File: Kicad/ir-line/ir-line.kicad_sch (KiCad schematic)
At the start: 28 parts, among them IC1 VISHAY-CNY70, IC2 VISHAY-CNY70, IC3 VISHAY-CNY70, IC4 VISHAY-CNY70, IC5 VISHAY-CNY70, IC6 TPS92612, IC7 TPS92612, K1 FRONT #1, K2 FRONT #2

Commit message: Draft
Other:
- note added: "DRAFT"
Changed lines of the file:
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@@
     (effects (font (size 1.27 1.27)) (justify left bottom))
+  )
+  (text "DRAFT" (at 210.82 190.5 0)
+    (effects (font (size 5 5)) (justify left bottom))
   )
   (text "(10n)" (at 154.94 109.22 0)

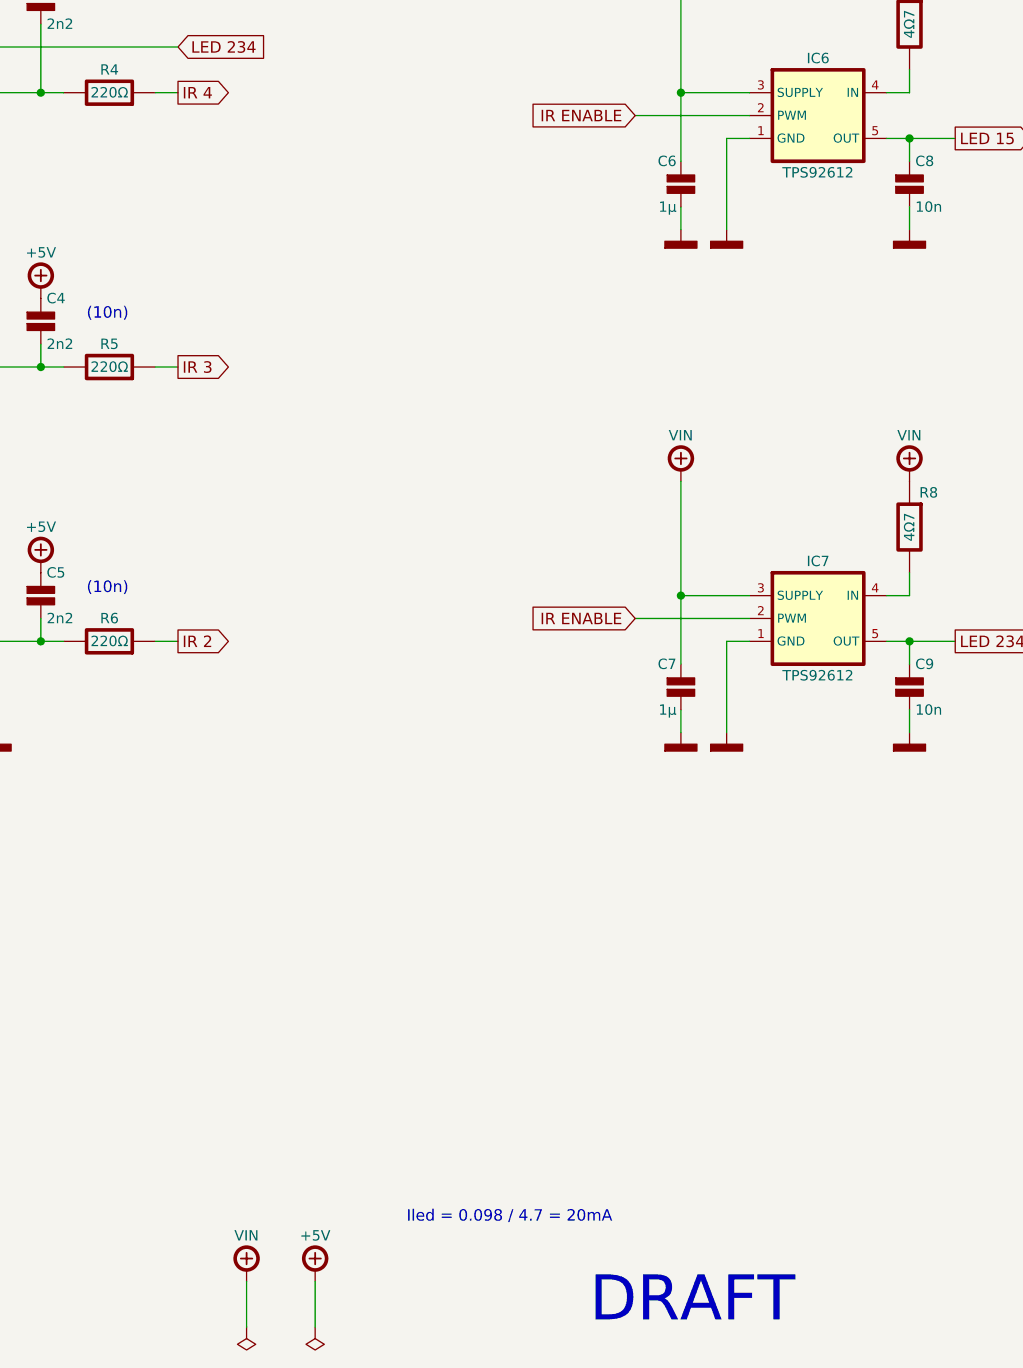
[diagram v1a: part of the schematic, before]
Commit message: Update IR Line
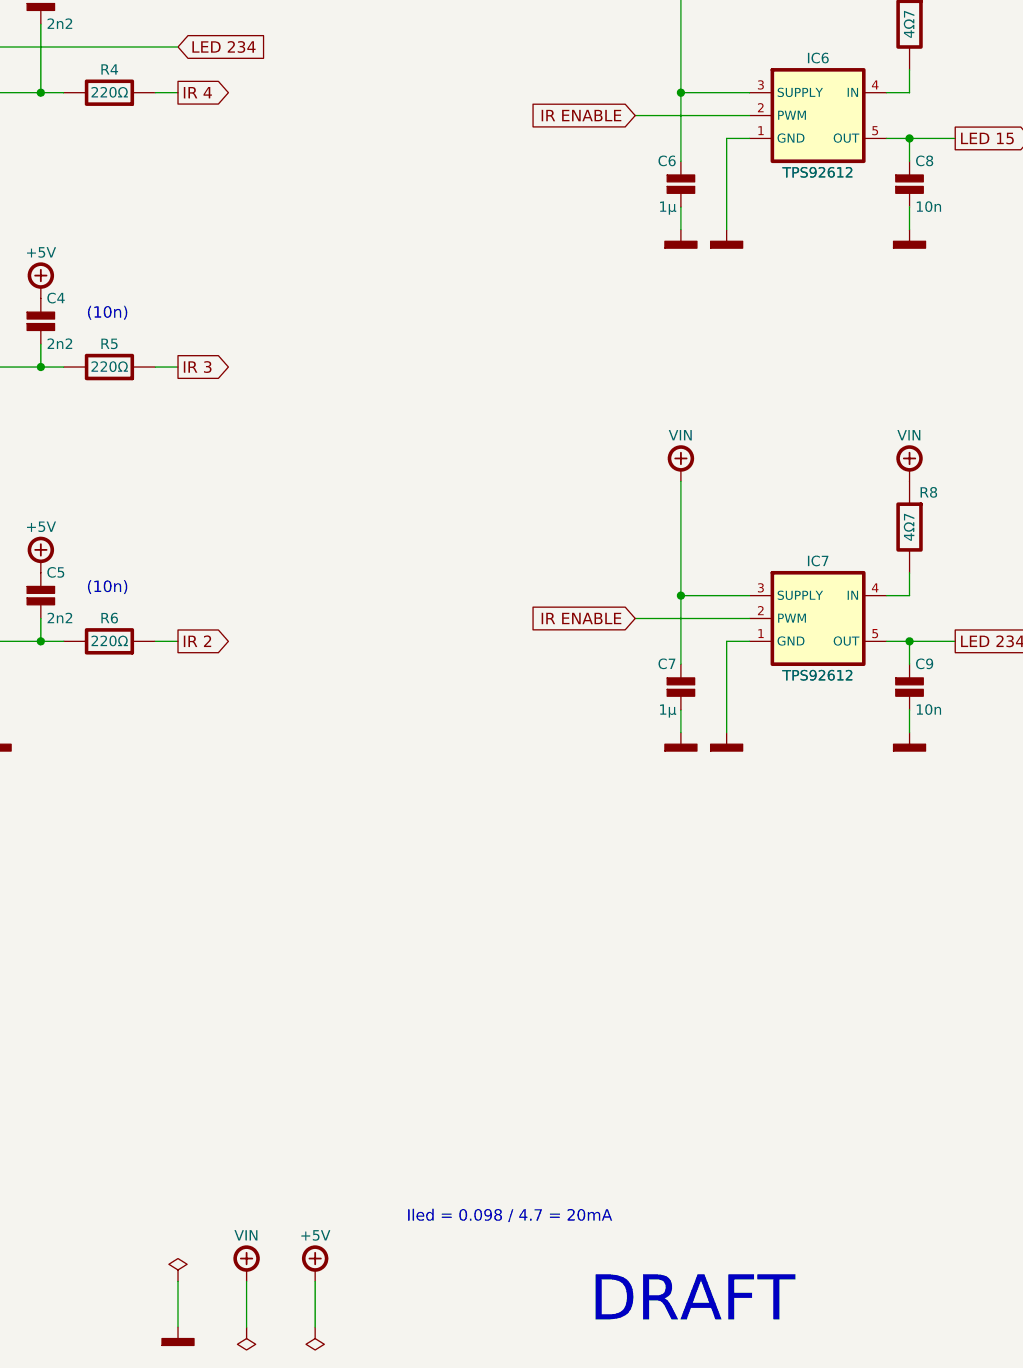
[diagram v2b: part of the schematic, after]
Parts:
- IC1, IC2, IC3, IC4, IC5: MOUSER 782-CNY70 -> (none); Mouser (none) -> 782-CNY70
- IC6, IC7: symbol tronixio:TPS92612 -> tronixio:TI-TPS92612; MOUSER 595-TPS92612DBVR -> (none); Mouser (none) -> 595-TPS92612DBVR; Name (none) -> TPS92612
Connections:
- net GND: now also IC1.4 (EMITTER), IC2.2 (CATHODE), IC2.4 (EMITTER), IC3.4 (EMITTER), IC4.4 (EMITTER), IC5.2 (CATHODE), IC5.4 (EMITTER); no longer IC1.3 (E), IC2.1 (K), IC2.3 (E), IC3.3 (E), IC4.3 (E), IC5.1 (K), IC5.3 (E)
- net LED 15: now also IC1.1 (ANODE); no longer IC1.4 (A)
- net LED 234: now also IC3.1 (ANODE); no longer IC3.4 (A)
- net at C3.2, R4.1: now also IC3.3 (COLLECTOR); no longer IC3.2 (C)
- net at C4.2, R5.1: now also IC4.3 (COLLECTOR); no longer IC4.2 (C)
- net at C1.2, R2.1: now also IC1.3 (COLLECTOR); no longer IC1.2 (C)
- net at C5.2, R6.1: now also IC5.3 (COLLECTOR); no longer IC5.2 (C)
- net at C2.2, R3.1: now also IC2.3 (COLLECTOR); no longer IC2.2 (C)
- net at IC4.1 (ANODE): now also IC3.2 (CATHODE); no longer IC5.4 (A)
- new net: IC1.2 (CATHODE), IC2.1 (ANODE)
- new net: IC4.2 (CATHODE), IC5.1 (ANODE)
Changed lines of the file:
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@@
     (stroke (width 0) (type solid) (color 0 0 0 0))
+  )
+  (wire (pts (xy 165.1 185.42) (xy 165.1 190.5))
+    (stroke (width 0) (type default) (color 0 0 0 0))
   )
   (wire (pts (xy 53.34 53.34) (xy 66.04 53.34))
@@
     )
     (property "Value" "VISHAY-CNY70" (id 1) (at 132.08 62.23 0)
-      (effects (font (size 1 1)) hide)
-    )
-    (property "Footprint" "tronixio:VISHAY-CNY70" (id 2) (at 132.08 62.23 0)
+      (effects (font (size 1.15 1.15)) hide)
+    )
+    (property "Footprint" "tronixio:VISHAY-CNY70" (id 2) (at 132.08 64.77 0)
       (effects (font (size 1 1)) hide)
     )
@@
       (effects (font (size 1 1)) hide)
     )
-    (property "MOUSER" "782-CNY70" (id 4) (at 132.08 69.85 0)
-      (effects (font (size 1 1)) hide)
-    )
     (property "Name" "CNY70" (id 5) (at 132.08 58.42 0)
       (effects (font (size 1.15 1.15)))
+    )
+    (property "Mouser" "782-CNY70" (id 6) (at 132.08 69.85 0)
+      (effects (font (size 1 1)) hide)
     )
     (pin "1")
@@
     (pin "1")
   )
-  (symbol (lib_id "tronixio:TPS92612") (at 236.22 111.76 0) (unit 1)
+  (symbol (lib_id "tronixio:TI-TPS92612") (at 236.22 111.76 0) (unit 1)
     (in_bom yes) (on_board yes)
     (property "Reference" "IC7" (id 0) (at 236.22 105.41 0)
@@
       (effects (font (size 1 1)) hide)
     )
-    (property "MOUSER" "595-TPS92612DBVR" (id 4) (at 236.22 127 0)
+    (property "Name" "TPS92612" (id 4) (at 236.22 118.11 0)
+      (effects (font (size 1.15 1.15)))
+    )
+    (property "Mouser" "595-TPS92612DBVR" (id 5) (at 236.22 129.54 0)
       (effects (font (size 1 1)) hide)
     )
@@
     )
     (property "Value" "VISHAY-CNY70" (id 1) (at 48.26 62.23 0)
-      (effects (font (size 1 1)) hide)
-    )
-    (property "Footprint" "tronixio:VISHAY-CNY70" (id 2) (at 48.26 62.23 0)
+      (effects (font (size 1.15 1.15)) hide)
+    )
+    (property "Footprint" "tronixio:VISHAY-CNY70" (id 2) (at 48.26 64.77 0)
       (effects (font (size 1 1)) hide)
     )
@@
       (effects (font (size 1 1)) hide)
     )
-    (property "MOUSER" "782-CNY70" (id 4) (at 48.26 69.85 0)
-      (effects (font (size 1 1)) hide)
-    )
     (property "Name" "CNY70" (id 5) (at 48.26 58.42 0)
       (effects (font (size 1.15 1.15)))
+    )
+    (property "Mouser" "782-CNY70" (id 6) (at 48.26 69.85 0)
+      (effects (font (size 1 1)) hide)
     )
     (pin "1")
@@
     (pin "1")
   )
+  (symbol (lib_id "tronixio:PWR_FLAG") (at 165.1 185.42 0) (unit 1)
+    (in_bom yes) (on_board yes) (fields_autoplaced)
+    (property "Reference" "#FLG01" (id 0) (at 165.1 187.325 0)
+      (effects (font (size 1.27 1.27)) hide)
+    )
+    (property "Value" "PWR_FLAG" (id 1) (at 165.1 189.23 0)
+      (effects (font (size 1.27 1.27)) hide)
+    )
+    (property "Footprint" "" (id 2) (at 165.1 185.42 0)
+      (effects (font (size 1.27 1.27)) hide)
+    )
+    (property "Datasheet" "~" (id 3) (at 165.1 185.42 0)
+      (effects (font (size 1.27 1.27)) hide)
+    )
+    (pin "1")
+  )
   (symbol (lib_id "tronixio:POWER-VIN") (at 220.98 40.64 0) (unit 1)
     (in_bom yes) (on_board yes)
@@
     (pin "2")
   )
+  (symbol (lib_id "tronixio:POWER-GND") (at 165.1 190.5 0) (unit 1)
+    (in_bom yes) (on_board yes)
+    (property "Reference" "#PWR015" (id 0) (at 165.1 195.58 0)
+      (effects (font (size 1 1)) hide)
+    )
+    (property "Value" "POWER-GND" (id 1) (at 165.1 198.12 0)
+      (effects (font (size 1 1)) hide)
+    )
+    (property "Footprint" "" (id 2) (at 165.1 190.5 0)
+      (effects (font (size 1 1)) hide)
+    )
+    (property "Datasheet" "" (id 3) (at 165.1 190.5 0)
+      (effects (font (size 1 1)) hide)
+    )
+    (pin "1")
+  )
   (symbol (lib_id "tronixio:POWER-GND") (at 226.06 124.46 0) (unit 1)
     (in_bom yes) (on_board yes)
@@
     (pin "1")
   )
-  (symbol (lib_id "tronixio:TPS92612") (at 236.22 55.88 0) (unit 1)
+  (symbol (lib_id "tronixio:TI-TPS92612") (at 236.22 55.88 0) (unit 1)
     (in_bom yes) (on_board yes)
     (property "Reference" "IC6" (id 0) (at 236.22 49.53 0)
@@
       (effects (font (size 1 1)) hide)
     )
-    (property "MOUSER" "595-TPS92612DBVR" (id 4) (at 236.22 71.12 0)
+    (property "Name" "TPS92612" (id 4) (at 236.22 62.23 0)
+      (effects (font (size 1.15 1.15)))
+    )
+    (property "Mouser" "595-TPS92612DBVR" (id 5) (at 236.22 73.66 0)
       (effects (font (size 1 1)) hide)
     )
@@
     )
     (property "Value" "VISHAY-CNY70" (id 1) (at 48.26 92.71 0)
-      (effects (font (size 1 1)) hide)
-    )
-    (property "Footprint" "tronixio:VISHAY-CNY70" (id 2) (at 48.26 92.71 0)
+      (effects (font (size 1.15 1.15)) hide)
+    )
+    (property "Footprint" "tronixio:VISHAY-CNY70" (id 2) (at 48.26 95.25 0)
       (effects (font (size 1 1)) hide)
     )
@@
       (effects (font (size 1 1)) hide)
     )
-    (property "MOUSER" "782-CNY70" (id 4) (at 48.26 100.33 0)
-      (effects (font (size 1 1)) hide)
-    )
     (property "Name" "CNY70" (id 5) (at 48.26 88.9 0)
       (effects (font (size 1.15 1.15)))
+    )
+    (property "Mouser" "782-CNY70" (id 6) (at 48.26 100.33 0)
+      (effects (font (size 1 1)) hide)
     )
     (pin "1")
@@
     )
     (property "Value" "VISHAY-CNY70" (id 1) (at 132.08 123.19 0)
-      (effects (font (size 1 1)) hide)
-    )
-    (property "Footprint" "tronixio:VISHAY-CNY70" (id 2) (at 132.08 123.19 0)
+      (effects (font (size 1.15 1.15)) hide)
+    )
+    (property "Footprint" "tronixio:VISHAY-CNY70" (id 2) (at 132.08 125.73 0)
       (effects (font (size 1 1)) hide)
     )
@@
       (effects (font (size 1 1)) hide)
     )
-    (property "MOUSER" "782-CNY70" (id 4) (at 132.08 130.81 0)
-      (effects (font (size 1 1)) hide)
-    )
     (property "Name" "CNY70" (id 5) (at 132.08 119.38 0)
       (effects (font (size 1.15 1.15)))
+    )
+    (property "Mouser" "782-CNY70" (id 6) (at 132.08 130.81 0)
+      (effects (font (size 1 1)) hide)
     )
     (pin "1")
@@
     )
     (property "Value" "VISHAY-CNY70" (id 1) (at 132.08 92.71 0)
-      (effects (font (size 1 1)) hide)
-    )
-    (property "Footprint" "tronixio:VISHAY-CNY70" (id 2) (at 132.08 92.71 0)
+      (effects (font (size 1.15 1.15)) hide)
+    )
+    (property "Footprint" "tronixio:VISHAY-CNY70" (id 2) (at 132.08 95.25 0)
       (effects (font (size 1 1)) hide)
     )
@@
       (effects (font (size 1 1)) hide)
     )
-    (property "MOUSER" "782-CNY70" (id 4) (at 132.08 100.33 0)
-      (effects (font (size 1 1)) hide)
-    )
     (property "Name" "CNY70" (id 5) (at 132.08 88.9 0)
       (effects (font (size 1.15 1.15)))
+    )
+    (property "Mouser" "782-CNY70" (id 6) (at 132.08 100.33 0)
+      (effects (font (size 1 1)) hide)
     )
     (pin "1")
@@
   )
   (symbol_instances
+    (path "/4442bbd3-d8c0-4204-a455-7ee1bc0d1e7f"
+      (reference "#FLG01") (unit 1) (value "PWR_FLAG") (footprint "")
+    )
     (path "/04e01352-a943-422f-843f-398a5122f31f"
       (reference "#FLG02") (unit 1) (value "PWR_FLAG") (footprint "")
@@
       (reference "#PWR014") (unit 1) (value "POWER-+5V") (footprint "")
     )
+    (path "/63a484a7-e75f-4f97-ac14-1ebad1b80741"
+      (reference "#PWR015") (unit 1) (value "POWER-GND") (footprint "")
+    )
     (path "/55d71a0a-a0b9-4237-b11f-ba473c6f7312"

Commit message: Update
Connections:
- net +5V renamed VCC
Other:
- note added: "VDD: 3V3 or 5V."
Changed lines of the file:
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@@
     (effects (font (size 1.27 1.27)) (justify left bottom))
   )
-  (text "Iled = 0.098 / 4.7 = 20mA" (at 213.36 179.07 180)
-    (effects (font (size 1.27 1.27)) (justify right bottom))
+  (text "VDD: 3V3 or 5V." (at 185.42 176.53 0)
+    (effects (font (size 1.27 1.27)) (justify left bottom))
   )
   (text "(10n)" (at 154.94 43.18 0)
@@
   (text "DRAFT" (at 210.82 190.5 0)
     (effects (font (size 5 5)) (justify left bottom))
+  )
+  (text "Iled = 0.098 / 4.7 = 20mA" (at 185.42 179.07 0)
+    (effects (font (size 1.27 1.27)) (justify left bottom))
   )
   (text "(10n)" (at 154.94 109.22 0)
@@
     (pin "1")
   )
-  (symbol (lib_id "tronixio:POWER-+5V") (at 149.86 76.2 0) (unit 1)
+  (symbol (lib_id "tronixio:POWER-VDD") (at 149.86 76.2 0) (unit 1)
     (in_bom yes) (on_board yes)
     (property "Reference" "#PWR013" (id 0) (at 149.86 86.36 0)
@@
       (effects (font (size 1 1)) hide)
     )
-    (property "Name" "+5V" (id 4) (at 149.86 71.12 0)
-      (effects (font (size 1.15 1.15)))
-    )
-    (pin "1")
-  )
-  (symbol (lib_id "tronixio:POWER-+5V") (at 66.04 40.64 0) (unit 1)
+    (property "Name" "VDD" (id 4) (at 149.86 71.12 0)
+      (effects (font (size 1.15 1.15)))
+    )
+    (pin "1")
+  )
+  (symbol (lib_id "tronixio:POWER-VDD") (at 66.04 40.64 0) (unit 1)
     (in_bom yes) (on_board yes)
     (property "Reference" "#PWR06" (id 0) (at 66.04 50.8 0)
       (effects (font (size 1 1)) hide)
     )
-    (property "Value" "POWER-+5V" (id 1) (at 66.04 53.34 0)
+    (property "Value" "" (id 1) (at 66.04 53.34 0)
       (effects (font (size 1 1)) hide)
     )
@@
       (effects (font (size 1 1)) hide)
     )
-    (property "Name" "+5V" (id 4) (at 66.04 35.56 0)
+    (property "Name" "VDD" (id 4) (at 66.04 35.56 0)
       (effects (font (size 1.15 1.15)))
     )
@@
     (pin "1")
   )
-  (symbol (lib_id "tronixio:POWER-+5V") (at 149.86 40.64 0) (unit 1)
+  (symbol (lib_id "tronixio:POWER-VDD") (at 149.86 40.64 0) (unit 1)
     (in_bom yes) (on_board yes)
     (property "Reference" "#PWR012" (id 0) (at 149.86 50.8 0)
@@
       (effects (font (size 1 1)) hide)
     )
-    (property "Name" "+5V" (id 4) (at 149.86 35.56 0)
+    (property "Name" "VDD" (id 4) (at 149.86 35.56 0)
       (effects (font (size 1.15 1.15)))
     )
@@
     (pin "5")
   )
-  (symbol (lib_id "tronixio:POWER-+5V") (at 180.34 185.42 0) (unit 1)
+  (symbol (lib_id "tronixio:POWER-VDD") (at 180.34 185.42 0) (unit 1)
     (in_bom yes) (on_board yes)
     (property "Reference" "#PWR017" (id 0) (at 180.34 195.58 0)
@@
       (effects (font (size 1 1)) hide)
     )
-    (property "Name" "+5V" (id 4) (at 180.34 180.34 0)
+    (property "Name" "VDD" (id 4) (at 180.34 180.34 0)
       (effects (font (size 1.15 1.15)))
     )
@@
     (pin "1")
   )
-  (symbol (lib_id "tronixio:POWER-+5V") (at 149.86 106.68 0) (unit 1)
+  (symbol (lib_id "tronixio:POWER-VDD") (at 149.86 106.68 0) (unit 1)
     (in_bom yes) (on_board yes)
     (property "Reference" "#PWR014" (id 0) (at 149.86 116.84 0)
@@
       (effects (font (size 1 1)) hide)
     )
-    (property "Name" "+5V" (id 4) (at 149.86 101.6 0)
+    (property "Name" "VDD" (id 4) (at 149.86 101.6 0)
       (effects (font (size 1.15 1.15)))
     )
@@
     (pin "1")
   )
-  (symbol (lib_id "tronixio:POWER-+5V") (at 66.04 76.2 0) (unit 1)
+  (symbol (lib_id "tronixio:POWER-VDD") (at 66.04 76.2 0) (unit 1)
     (in_bom yes) (on_board yes)
     (property "Reference" "#PWR07" (id 0) (at 66.04 86.36 0)
@@
       (effects (font (size 1 1)) hide)
     )
-    (property "Name" "+5V" (id 4) (at 66.04 71.12 0)
+    (property "Name" "VDD" (id 4) (at 66.04 71.12 0)
       (effects (font (size 1.15 1.15)))
     )
@@
     (pin "2")
   )
-  (symbol (lib_id "tronixio:POWER-+5V") (at 91.44 144.78 0) (unit 1)
+  (symbol (lib_id "tronixio:POWER-VDD") (at 91.44 144.78 0) (unit 1)
     (in_bom yes) (on_board yes)
     (property "Reference" "#PWR08" (id 0) (at 91.44 154.94 0)
@@
       (effects (font (size 1 1)) hide)
     )
-    (property "Name" "+5V" (id 4) (at 91.44 139.7 0)
-      (effects (font (size 1.15 1.15)))
-    )
+    (property "Name" "VDD" (id 4) (at 91.44 139.7 0)
+      (effects (font (size 1.15 1.15)))
+    )

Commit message: Update
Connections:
- net VCC renamed +5V
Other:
- moved on the sheet: C1, C2, C3, C4, C5, C6, C7, C8, C9, IC1, IC2, IC3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

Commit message: Update
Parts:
- C1, C2, C3, C4, C5: footprint tronixio:CAPACITOR-1206 -> tronixio:CAPACITOR-SMD-1206; symbol tronixio:C-1206 -> tronixio:CAPACITOR-1206-2N2-10P-X7R; Mouser (none) -> 80-C1206C222K5R; Tolerance (none) -> 10%; Voltage (none) -> 50V
- C6, C7: footprint tronixio:CAPACITOR-1206 -> tronixio:CAPACITOR-SMD-1206; symbol tronixio:C-1206 -> tronixio:CAPACITOR-1206-1U-10P-X7R; Mouser (none) -> 80-C1206C105K4R; Tolerance (none) -> 10%; Voltage (none) -> 16V
- C8, C9: footprint tronixio:CAPACITOR-1206 -> tronixio:CAPACITOR-SMD-1206; symbol tronixio:C-1206 -> tronixio:CAPACITOR-1206-10N-20P-X7R; Mouser (none) -> 80-C1206C103M5R; Tolerance (none) -> 20%; Voltage (none) -> 50V
- H1, H2: value MOUNTING-HOLE-MASK-3MM -> MOUNTING-HOLE-3MM-MASK; footprint tronixio:M3-MASK -> tronixio:MOUNTING-HOLE-3MM-MASK; symbol tronixio:MOUNTING-HOLE-MASK-3MM -> tronixio:MOUNTING-HOLE-3MM-MASK
- IC1, IC2, IC3, IC4, IC5: value VISHAY-CNY70 -> CNY70; Name CNY70 -> (none)
- IC6, IC7: symbol tronixio:TI-TPS92612 -> tronixio:TI-TPS92612-SOT; Name TPS92612 -> (none)
- K1, K2: MOUSER 538-53253-0570 -> (none); Mouser (none) -> 538-53253-0570
- R1: value 100K -> 100k; footprint tronixio:RESISTOR-1206 -> tronixio:RESISTOR-SMD-1206; symbol tronixio:R-1206 -> tronixio:RESISTOR-1206-100K-5P; Mouser (none) -> 660-RK73B2BTTDD104J; Tolerance (none) -> 5%
- R2, R3, R4, R5, R6: footprint tronixio:RESISTOR-1206 -> tronixio:RESISTOR-SMD-1206; symbol tronixio:R-1206 -> tronixio:RESISTOR-1206-220R-5P; Mouser (none) -> 660-RK73B2BTTDD221J; Tolerance (none) -> 5%
- R7, R8: value 4Ω7 -> 220Ω; footprint tronixio:RESISTOR-1206 -> tronixio:RESISTOR-SMD-1206; symbol tronixio:R-1206 -> tronixio:RESISTOR-1206-220R-5P; Mouser (none) -> 660-RK73B2BTTDD221J; Tolerance (none) -> 5%
